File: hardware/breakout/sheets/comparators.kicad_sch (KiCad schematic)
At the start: 17 parts, among them U54 LM339, U55 MCP4728

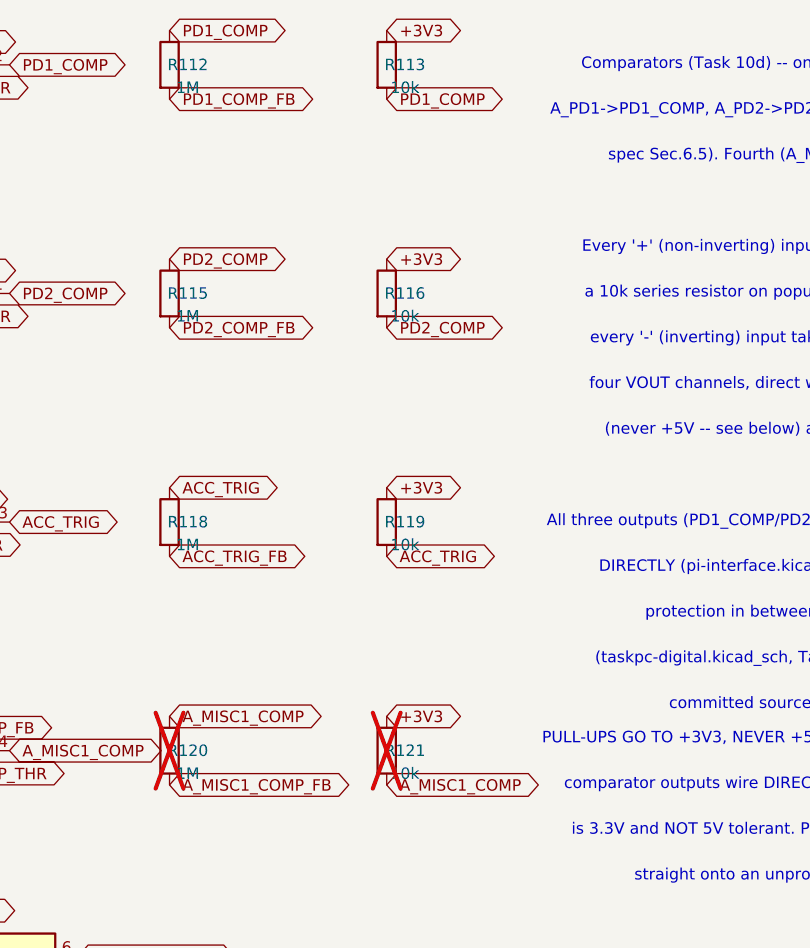
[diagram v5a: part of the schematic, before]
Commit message: fix(hardware): the analog front-end corrections (F3, M1, M2, M4; D1 recorded)
Five findings, both photodiode channels each.

F3 -- THE TRANSIMPEDANCE STAGE SATURATED. R38/R40 1M -> 180k. An FDS100 is
13 mm2 at 0.30 A/W, so a display flip patch at ~0.29 mW/cm2 delivers
~11.3 uA -- and 11.3 uA x 1M demands 11.3 V, twice this board's +-5 V analog
convention and past both NI's and Intan's input range. The stage clipped
long before full scale.

That matters more than a gain error sounds. The flat part is the BRIGHT
part, and the edge these channels exist to time is what survives, so the
defect would have looked like "it works" on a scope. 180k puts peak white
near 2.0 V, which also lands inside the DAC's own 0-2.048 V span after D1.

The DNP parallel trim positions the finding asks for are fitted (R196/R197,
unpopulated). A resistor pad rather than a jumper, deliberately: gain rests
on an estimate of display irradiance rather than a measurement, so bring-up
needs a way to move it, but a mechanical contact at a 180k summing junction
would be a leakage and noise liability.

M1 -- IT WAS ALSO UNDER-COMPENSATED. C48/C50 3.3pF -> 22pF. 3.3pF was
fitted for a 1M stage against an assumed 300-500 pF of input capacitance.
Thorlabs publish the FDS100's capacitance only at 20 V bias (24 pF); this
design is forced into ZERO bias by the no-power-in-the-booth constraint,
where it is at maximum and unpublished -- estimated 130-380 pF, and 440-900
pF with 3-5 m of coax.

22pF at 180k is deliberate over-compensation, not a fit: stable to 5.5 nF
of input capacitance (~50 m of coax) at -3 dB = 40 kHz, still four times
what these channels need. The stage stops depending on cable length and on
a diode capacitance nobody can look up. The BOM now calls for C0G/NP0 on
these two rather than X7R -- a compensation capacitor whose value moves
with bias or temperature is not doing this job.

M2 -- THE MUX TAPPED THE WRONG NODE. The eight muxes' S7/S8 inputs move
from A_PD1/A_PD2 to A_PD1_NI_BUF/A_PD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
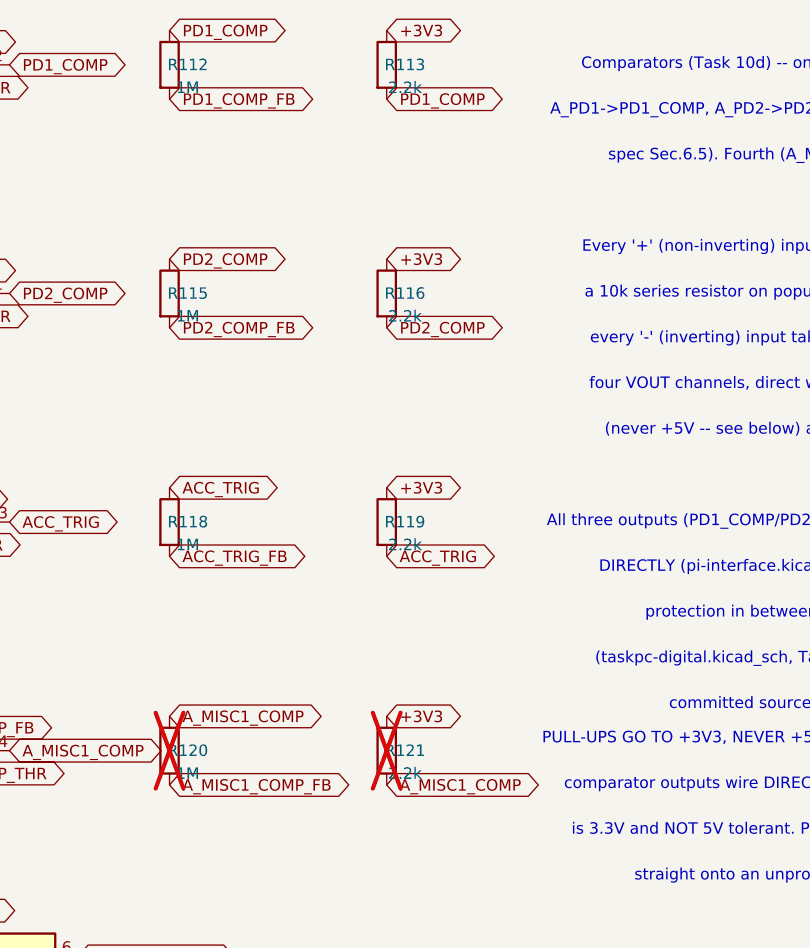
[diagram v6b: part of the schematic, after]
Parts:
- R113, R116, R119, R121: value 10k -> 2.2k
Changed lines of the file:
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@@
 			(effects (font (size 1.27 1.27)))
 		)
-		(property "Value" "10k"
+		(property "Value" "2.2k"
 			(at 126.49199999999999 22.86 0)
 			(effects (font (size 1.27 1.27)))
@@
 			(effects (font (size 1.27 1.27)))
 		)
-		(property "Value" "10k"
+		(property "Value" "2.2k"
 			(at 126.49199999999999 48.26 0)
 			(effects (font (size 1.27 1.27)))
@@
 			(effects (font (size 1.27 1.27)))
 		)
-		(property "Value" "10k"
+		(property "Value" "2.2k"
 			(at 126.49199999999999 73.66000000000001 0)
 			(effects (font (size 1.27 1.27)))
@@
 			(effects (font (size 1.27 1.27)))
 		)
-		(property "Value" "10k"
+		(property "Value" "2.2k"
 			(at 126.49199999999999 99.06 0)
 			(effects (font (size 1.27 1.27)))
